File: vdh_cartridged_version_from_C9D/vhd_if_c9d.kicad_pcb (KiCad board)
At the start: 2 copper layers, 100 x 152 mm, 58 parts, among them IC1 80C49C, IC10 74LS04, IC12 74H004P, IC2 NEC D8255AC-2, IC3 27C256, IC6 74LS30, IC8 74LS32, IC9 74LS02, J1 Conn_02x25_Odd_Even, J3 DB15_Female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

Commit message: Add files via upload
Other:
- board text added: "VHD Card by Popolon_"
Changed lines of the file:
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@@
   (general
     (thickness 1.6)
-    (drawings 15)
+    (drawings 16)
     (tracks 1229)
     (zones 0)
@@
     )
   )
+  (gr_text "VHD Card by Popolon_" (at 85.4075 25.019) (layer F.SilkS)
+    (effects (font (size 1.5 1.5) (thickness 0.3)))
+  )
   (gr_line (start 71.6915 104.8385) (end 170.561 104.8385) (layer F.SilkS) (width 0.12))

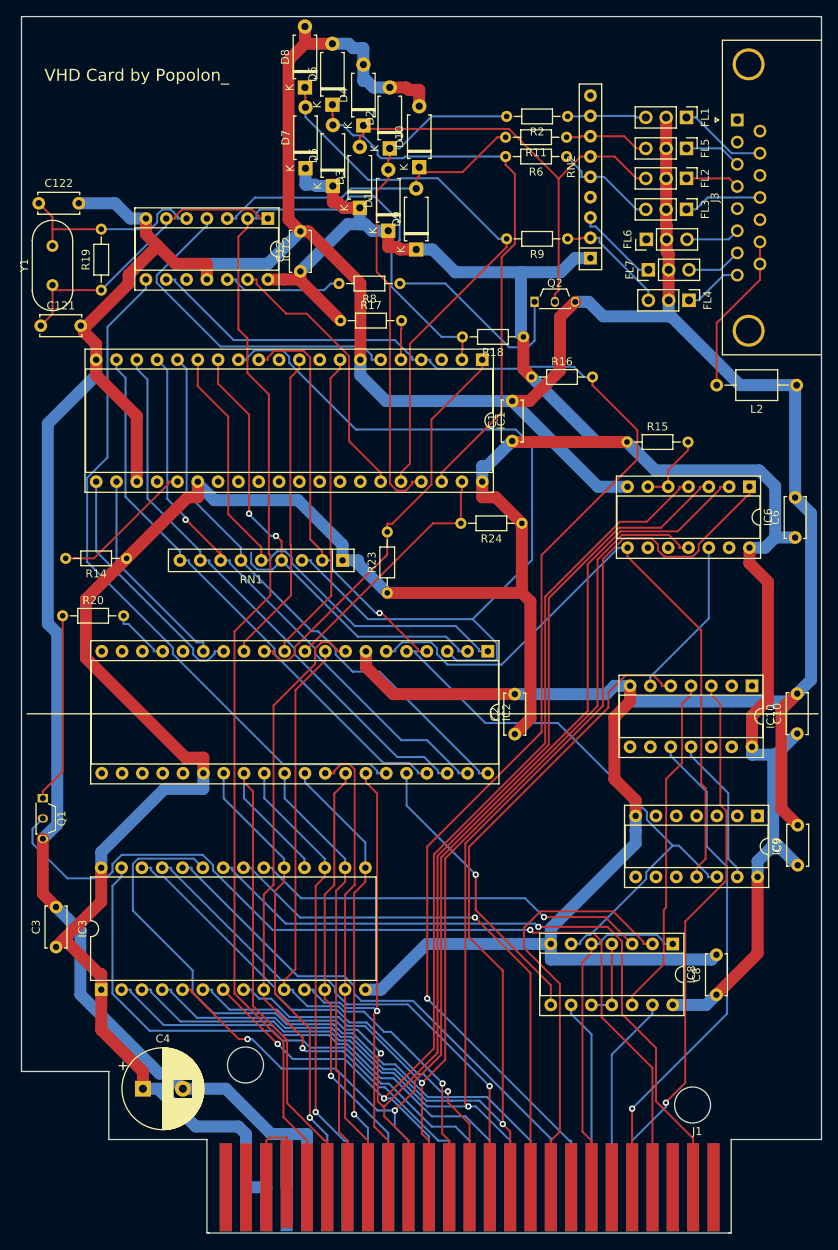
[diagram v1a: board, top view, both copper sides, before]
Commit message: corrected CLK signal connection
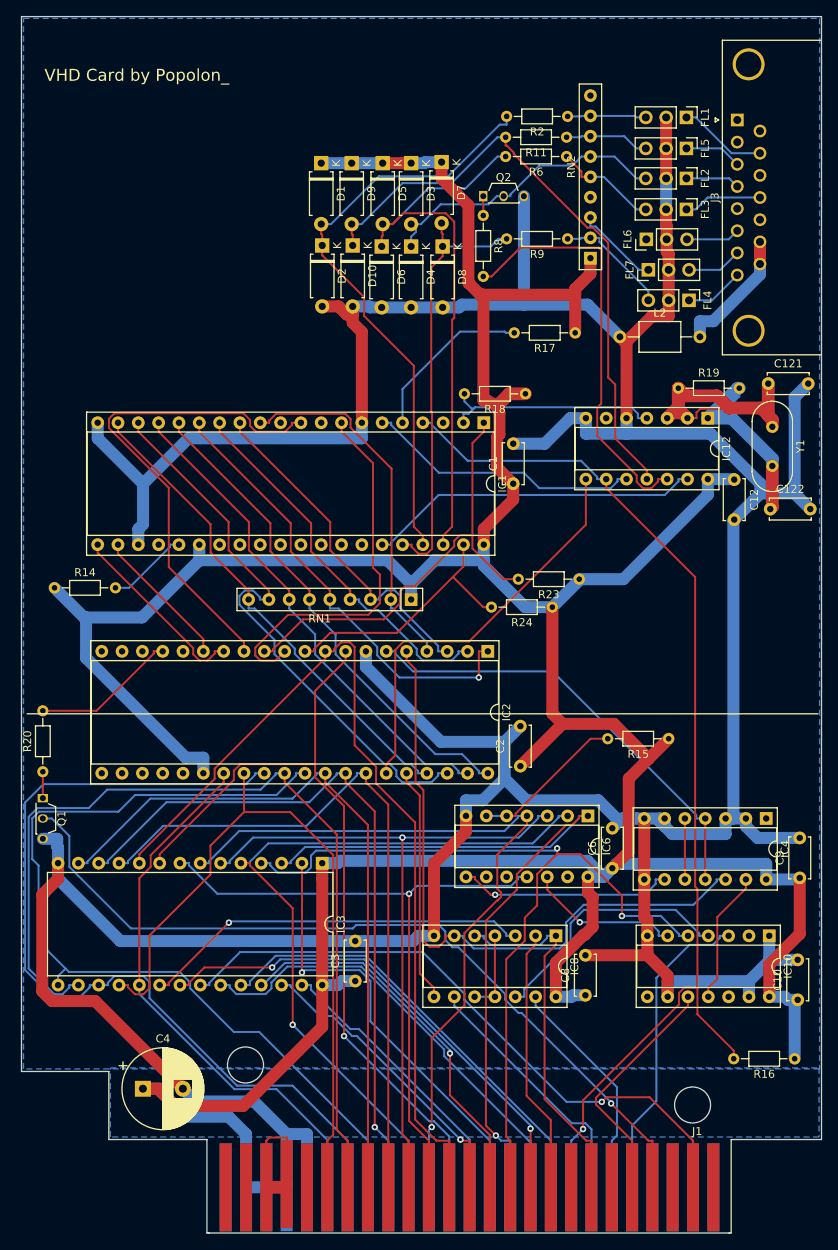
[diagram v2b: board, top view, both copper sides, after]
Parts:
- moved C122 99.1 mm to (164.6, 79.2)
- moved Y1 91.7 mm to (164.8, 69.0), turned to 270 degrees
- moved R16 91.3 mm to (167.6, 148.0), turned to 180 degrees
- moved C121 91.2 mm to (164.3, 63.6)
- moved R19 73.2 mm to (153.1, 64.1), turned to 0 degrees
- moved IC12 60.4 mm to (156.8, 67.9)
- moved C12 60.2 mm to (160.1, 75.6), turned to 270 degrees
- moved C6 47.2 mm to (144.8, 124.1)
- moved IC6 45.8 mm to (141.8, 117.6)
- moved C3 37.6 mm to (112.7, 138.2)
- moved R15 37.4 mm to (151.9, 108.0), turned to 180 degrees
- moved C10 33.3 mm to (168.0, 140.6)
- moved IC3 31.8 mm to (108.6, 123.5), turned to 270 degrees
- moved IC10 31.3 mm to (164.5, 132.6)
- moved R17 29.4 mm to (140.2, 57.2), turned to 180 degrees
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- renumbered IC9 to IC4
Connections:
- IC10 pad 1: (no net) -> GND
- IC10 pad 13: (no net) -> GND
- IC10 pad 9: (no net) -> GND
- IC12 pad 1: Net-(C121-Pad1) -> Net-(C122-Pad1)
- IC12 pad 10: (no net) -> Net-(IC1-Pad6)
- IC12 pad 11: GND -> Net-(D10-Pad1)
- IC12 pad 2: CLK -> Net-(C121-Pad1)
- IC12 pad 3: Net-(D10-Pad1) -> Net-(C121-Pad1)
- IC12 pad 4: Net-(IC1-Pad6) -> CLK
- IC12 pad 5: Net-(C122-Pad1) -> GND
- IC12 pad 6: Net-(C121-Pad1) -> (no net)
- IC4 pad 10: (no net) -> Net-(IC4-Pad10)
- IC4 pad 2: (no net) -> GND
- IC4 pad 3: (no net) -> GND
- IC4 pad 4: (no net) -> Net-(IC2-Pad6)
- IC4 pad 5: (no net) -> Net-(IC4-Pad10)
- IC4 pad 6: (no net) -> GND
- IC4 pad 8: (no net) -> GND
- IC4 pad 9: (no net) -> Net-(IC4-Pad9)
- IC6 pad 8: Net-(IC2-Pad6) -> Net-(IC4-Pad9)
- J1 pad 42: CLK -> (no net)
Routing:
- net CLK: track 173.7 -> 27.8 mm
- net A7: track 161.0 -> 95.7 mm
- net Net-(IC1-Pad13): track 105.0 -> 43.5 mm
- net D4: track 55.9 -> 116.5 mm
- net D3: track 56.2 -> 112.5 mm, vias 1 -> 0
- net A4: track 142.3 -> 87.6 mm
- net D5: track 57.2 -> 111.2 mm, vias 1 -> 0
- net A5: track 143.4 -> 93.4 mm, vias 2 -> 1
- net GND: track 596.3 -> 547.8 mm
- net A2: track 128.7 -> 83.9 mm
- net RESET_: track 181.1 -> 137.7 mm
- net A3: track 134.5 -> 95.5 mm, vias 2 -> 1
- net A14: track 74.3 -> 35.2 mm
- net Net-(IC12-Pad12): track 15.0 -> 52.4 mm
- net Net-(D10-Pad1): track 40.9 -> 77.0 mm
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- added copper zone on B.Cu, net GND
